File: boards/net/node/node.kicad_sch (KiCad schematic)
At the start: 60 parts, among them J1 N, J2 E, J3 S, J4 W, J5 SENSOR, J6 PROG, SW1 SW-18010P, U1 RP2040, U2 W25Q16JVSSIQ, U3 VL53L0CXV0DH/1, U4 ME6211C33M5G, Y1 12MHz

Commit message: net/node: link connectors centred and aligned for tiling; U1 caps to 0402
J1..J4 now sit with pin 2 exactly on each edge's centre line (24.0 on
the 48 x 48 board), so a node's W/S connectors line up with its
neighbours' E/N connectors when the net is tiled by translation.
pcb.py derives the rows from the board centre and refuses to generate
a board whose facing rows are misaligned or off-centre.

To free the west edge for J4, the U1 decoupling caps C10/C15 (100 nF,
C307331) and C11/C13 (1 uF, C52923) are now 0402, packed beside pins
43-45: pin-to-cap tracks went from 2.6-8.0 mm to 1.4-2.9 mm. C9 moved
0.5 mm and DM/DP re-routed; R15/R16, the crystal, pogo pads and M2
holes are unchanged. J5 moved 0.07 mm east to clear J3's courtyard,
leaving two silk_edge_clearance warnings (documented).

README: tiling rule and half-twist cable note, 0402 decision, variant
BOM command groups like the jobset so 0402/0603 parts stay separate.

Co-Authored-By: Claude Opus 5.5 <noreply@anthropic.com>
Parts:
- C10, C15: footprint Capacitor_SMD:C_0603_1608Metric -> Capacitor_SMD:C_0402_1005Metric; LCSC C14663 -> C307331; MPN CC0603KRX7R9BB104 -> CL05B104KB54PNC; Manufacturer Yageo -> Samsung
- C11, C13: footprint Capacitor_SMD:C_0603_1608Metric -> Capacitor_SMD:C_0402_1005Metric; LCSC C15849 -> C52923; MPN CL10A105KB8NNNC -> CL05A105KA5NQNC
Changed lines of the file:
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@@
 			)
 		)
-		(property "Footprint" "Capacitor_SMD:C_0603_1608Metric"
+		(property "Footprint" "Capacitor_SMD:C_0402_1005Metric"
 			(at 99.06 205.74 0)
 			(effects
@@
 			)
 		)
-		(property "Description" "100 nF X7R 50 V"
+		(property "Description" "100 nF X7R 50 V 0402"
 			(at 99.06 205.74 0)
 			(effects
@@
 			)
 		)
-		(property "MPN" "CC0603KRX7R9BB104"
+		(property "MPN" "CL05B104KB54PNC"
 			(at 99.06 205.74 0)
 			(effects
@@
 			)
 		)
-		(property "Manufacturer" "Yageo"
+		(property "Manufacturer" "Samsung"
 			(at 99.06 205.74 0)
 			(effects
@@
 			)
 		)
-		(property "LCSC" "C14663"
+		(property "LCSC" "C307331"
 			(at 99.06 205.74 0)
 			(effects
@@
 			)
 		)
-		(property "Footprint" "Capacitor_SMD:C_0603_1608Metric"
+		(property "Footprint" "Capacitor_SMD:C_0402_1005Metric"
 			(at 106.68 205.74 0)
 			(effects
@@
 			)
 		)
-		(property "Description" "1 uF X5R 50 V"
+		(property "Description" "1 uF X5R 25 V 0402"
 			(at 106.68 205.74 0)
 			(effects
@@
 			)
 		)
-		(property "MPN" "CL10A105KB8NNNC"
+		(property "MPN" "CL05A105KA5NQNC"
 			(at 106.68 205.74 0)
 			(effects
@@
 			)
 		)
-		(property "LCSC" "C15849"
+		(property "LCSC" "C52923"
 			(at 106.68 205.74 0)
 			(effects
@@
 			)
 		)
-		(property "Footprint" "Capacitor_SMD:C_0603_1608Metric"
+		(property "Footprint" "Capacitor_SMD:C_0402_1005Metric"
 			(at 127 205.74 0)
 			(effects
@@
 			)
 		)
-		(property "Description" "1 uF X5R 50 V"
+		(property "Description" "1 uF X5R 25 V 0402"
 			(at 127 205.74 0)
 			(effects
@@
 			)
 		)
-		(property "MPN" "CL10A105KB8NNNC"
+		(property "MPN" "CL05A105KA5NQNC"
 			(at 127 205.74 0)
 			(effects
@@
 			)
 		)
-		(property "LCSC" "C15849"
+		(property "LCSC" "C52923"
 			(at 127 205.74 0)
 			(effects
@@
 			)
 		)
-		(property "Footprint" "Capacitor_SMD:C_0603_1608Metric"
+		(property "Footprint" "Capacitor_SMD:C_0402_1005Metric"
 			(at 142.24 205.74 0)
 			(effects
@@
 			)
 		)
-		(property "Description" "100 nF X7R 50 V"
+		(property "Description" "100 nF X7R 50 V 0402"
 			(at 142.24 205.74 0)
 			(effects
@@
 			)
 		)
-		(property "MPN" "CC0603KRX7R9BB104"
+		(property "MPN" "CL05B104KB54PNC"
 			(at 142.24 205.74 0)
 			(effects
@@
 			)
 		)
-		(property "Manufacturer" "Yageo"
+		(property "Manufacturer" "Samsung"
 			(at 142.24 205.74 0)
 			(effects
@@
 			)
 		)
-		(property "LCSC" "C14663"
+		(property "LCSC" "C307331"
 			(at 142.24 205.74 0)
 			(effects

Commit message: net/node: re-floorplan (MCU centre, peripherals in corners); J5 removed
U1 (rotated 180) and its support (decoupling, crystal, flash, LDO,
USB series R) now fill the centre between the four edge-centred link
connectors; peripherals take the corners: BZ1 NE, VL53L0X SE, pogo
pads J6 SW, SW1 NW. LED D2 sits just NE of U1. The 5 V ring is closed.

J5 (1x7 sensor header) is removed: its courtyard fits no corner and it
carried the longest run (SENS_AIN). GPIO26 is a no-connect; the bare
variant is now a sensorless relay node.

Mounting holes: no pad, via or footprint within 3.7 mm of a hole
centre (C2 had been 3.08 mm from H1; an M2 washer is 5 mm OD),
enforced by annulus keepouts (pcbgen.keepout r_in/pads/footprints/
tracks) and a pcb.py assertion. Crystal copper 23.3 -> 16.2 mm, USB
pair ~26 -> ~23 mm; make check: 0 violations, 0 warnings.

Co-Authored-By: Claude Opus 5.5 <noreply@anthropic.com>
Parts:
- removed J5: SENSOR, Connector_PinHeader_2.54mm:PinHeader_1x07_P2.54mm_Vertical, symbol Connector_Generic:Conn_01x07
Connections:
- net SENS_AIN: no longer names the net of U1.38 (GPIO26/ADC0)
- no-connect marks 21 -> 22
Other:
- note added: "Sensor. U3 = default variant, SW1 = "vib" variant, "bare" = no sensor (relay-only node)."
- note removed: "Sensor port. J5 takes off-board modules (LD2410, AM312 PIR, I2C breakouts). U3 = default variant, SW1 = "vib" variant, "bare" = header only."
- title: Net node: RP2040, 4 neighbour links, RGB LED, piezo, sensor port -> Net node: RP2040, 4 neighbour links, RGB LED, piezo, sensor

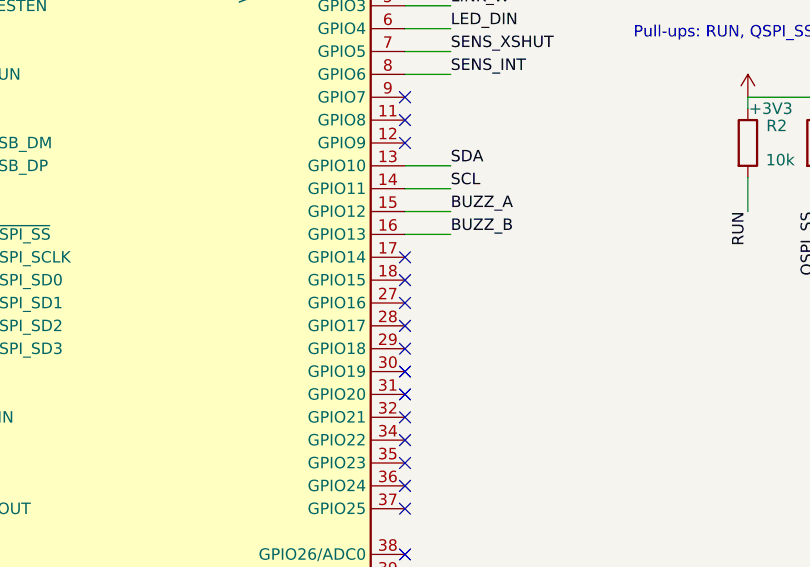
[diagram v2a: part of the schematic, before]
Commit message: net/node: isolate the crystal (buzzer to GPIO18/19, guard pour, 1 mm rule); J6 centred
The piezo drive moved from GPIO12/13 (pins 15/16, four pins from
XIN/XOUT) to GPIO18/19 (PWM slice 1 A/B, pins 29/30), routed on B.Cu
under U1 to BZ1; BUZZ_B went from 0.55 to 2.0 mm from crystal copper.

Every other non-GND net now keeps >= 1.0 mm (same layer, edge to edge)
from the crystal nets and the LED nets and all D4 pads >= 2.0 mm,
checked by generate/xtal_check.py (tracks, arcs with sagitta margin,
vias, pads, zones; rejects unmodelled copper) and asserted from
pcb.py. Known exemption: the IOVDD/DVDD escapes inside U1's pin field.
A notched F.Cu GND guard pour surrounds Y1/C1/C2/R1, stitched to In1
by 19 vias, asserted free of foreign copper. C19 now sits at D2's VDD
pin (LED loop 15.5 -> 8.7 mm).

J6 pogo pads centred in the SW corner (margins to J3/J4/H3 ring
0.57/0.58/0.60 mm); USB pair 22.0/19.8 mm; README jig coordinates
updated. make check: 0 violations, 0 warnings.

Co-Authored-By: Claude Opus 5.5 <noreply@anthropic.com>
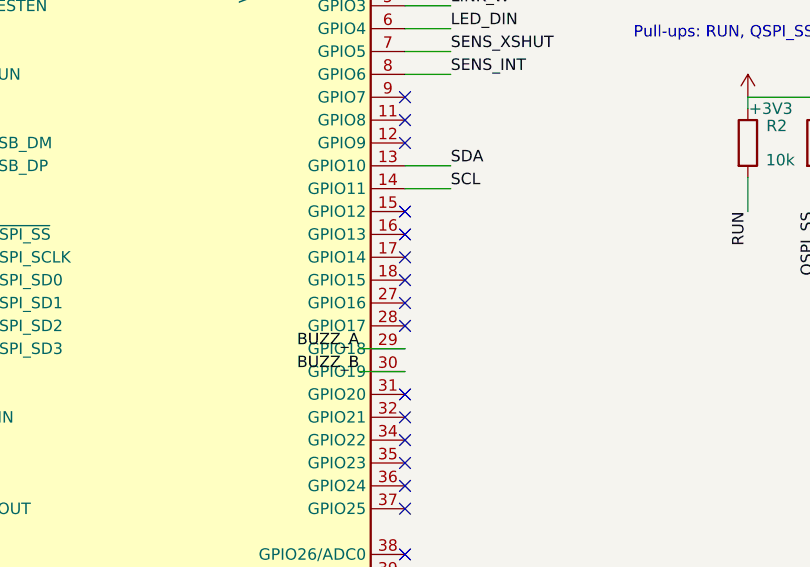
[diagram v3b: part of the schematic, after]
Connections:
- net BUZZ_A: now also U1.29 (GPIO18); no longer U1.15 (GPIO12)
- net BUZZ_B: now also U1.30 (GPIO19); no longer U1.16 (GPIO13)
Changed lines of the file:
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@@
 	(wire
 		(pts
-			(xy 139.7 119.38)
-			(xy 144.78 119.38)
+			(xy 139.7 134.62)
+			(xy 134.62 134.62)
 		)
 		(stroke
@@
 	)
 	(label "BUZZ_A"
-		(at 144.78 119.38 0)
-		(effects
-			(font
-				(size 1.27 1.27)
-			)
-			(justify left bottom)
-		)
-	)
-	(wire
-		(pts
-			(xy 139.7 121.92)
-			(xy 144.78 121.92)
+		(at 134.62 134.62 180)
+		(effects
+			(font
+				(size 1.27 1.27)
+			)
+			(justify right bottom)
+		)
+	)
+	(wire
+		(pts
+			(xy 139.7 137.16)
+			(xy 134.62 137.16)
 		)
 		(stroke
@@
 	)
 	(label "BUZZ_B"
-		(at 144.78 121.92 0)
-		(effects
-			(font
-				(size 1.27 1.27)
-			)
-			(justify left bottom)
+		(at 134.62 137.16 180)
+		(effects
+			(font
+				(size 1.27 1.27)
+			)
+			(justify right bottom)
 		)
 	)
@@
 	)
 	(no_connect
+		(at 139.7 119.38)
+	)
+	(no_connect
+		(at 139.7 121.92)
+	)
+	(no_connect
 		(at 139.7 124.46)
 	)
@@
 	)
 	(no_connect
-		(at 139.7 134.62)
-	)
-	(no_connect
-		(at 139.7 137.16)
-	)
-	(no_connect

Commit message: net/node: four corner LEDs; pre-order panel fixes (BOOT 1k, TVS, USB Schottky)
Four WS2812B-2020-V6 (D1..D4, C52917434), one per corner, 4.0 mm in
from an edge and 8.8 mm from the corner, chained NE->NW->SW->SE on
GPIO4, so a node shows the direction a pattern moves (2x2 sub-pixels).
Each has its own 100 nF 0402. The LEDs run from +5V through
U5 SN74AHCT1G125 (C7484) as level shifter; the 1N4148W drop diode is
gone (at LED idle current it no longer guaranteed VIH). Board stays
48 x 48; budget ~215 mA/node full white.

Fixes from the cross-model pre-order review:
- R19 1 k between QSPI_SS and the BOOT pogo pad, at the flash (RP2040
  hardware design guide p.9); J6.8 no longer shorts QSPI_SS.
- D5 SMF5.0A TVS on +5V at the LDO input (energy sink; limits
  documented, measure the plug transient on first boards).
- D6 B5819W from the jig's USB 5 V to +5V, so a powered net cannot
  backfeed the host.
- J1-J4 and SW1 out of the position files (hand-soldered);
  pcbgen carries base exclusions into variants (+ test).
- J6 vias moved out of the pogo pads; piezo drive modes without DC.

make check: 0 violations, 0 warnings; make parts --boards 30 clean.

Co-Authored-By: Claude Opus 5.5 <noreply@anthropic.com>
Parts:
- removed D1: 1N4148W, Diode_SMD:D_SOD-123, symbol Device:D
- added C23, C24, C25, C26: 100n, Capacitor_SMD:C_0402_1005Metric, symbol Device:C
- added D1, D3: WS2812B-2020-V6, LED_SMD:LED_WS2812B-2020_PLCC4_2.0x2.0mm, symbol LED:WS2812B-2020
- added D5: SMF5.0A, Diode_SMD:D_SOD-123F, symbol Device:D_Zener
- added D6: B5819W, Diode_SMD:D_SOD-123, symbol Device:D_Schottky
- added R19: 1k, Resistor_SMD:R_0603_1608Metric, symbol Device:R
- added U5: 74AHCT1G125, Package_TO_SOT_SMD:SOT-23-5, symbol 74xGxx:74AHCT1G125
- C19: footprint Capacitor_SMD:C_0603_1608Metric -> Capacitor_SMD:C_0402_1005Metric; LCSC C14663 -> C307331; MPN CC0603KRX7R9BB104 -> CL05B104KB54PNC; Manufacturer Yageo -> Samsung
- D4: now fitted
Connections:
- net LED_VDD is gone; now on net +5V: C19.1, D2.4 (VDD), D4.4 (VDD)
- net +5V: now also C23.1, C24.1, C25.1, C26.1, D1.4 (VDD), D3.4 (VDD), D5.1 (K), D6.1 (K), U5.5 (VCC); no longer J6.7 (Pin_7)
- net GND: now also C23.2, C24.2, C25.2, C26.2, D1.2 (VSS), D3.2 (VSS), D5.2 (A), U5.1, U5.3 (GND)
- net LED_DIN: now also D1.3 (DIN), U5.4; no longer D2.3 (DIN), U1.6 (GPIO4)
- net QSPI_SS: now also R19.1; no longer J6.8 (Pin_8)
- net LED_CH2: now reaches D2.1 (DOUT)
- net LED_CH2: now also D3.3 (DIN); no longer D4.3 (DIN)
- new net: D6.2 (A), J6.7 (Pin_7)
- new net BOOT: J6.8 (Pin_8), R19.2
- new net LED_CH1: D1.1 (DOUT), D2.3 (DIN)
- new net LED_CH3: D3.1 (DOUT), D4.3 (DIN)
- new net LED_DATA: U1.6 (GPIO4), U5.2
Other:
- note added: "Corner LEDs, chain D1 NE -> D2 NW -> D3 SW -> D4 SE (pixel 0..3), all on +5V. U5 (AHCT, VIH 2.0 V) shifts the 3.3 V data to 5 V: WS2812B-2020-V6 VIH = 0.55 VDD."
- note removed: "D1 drops the LED supply to ~4.3 V: WS2812B-2020-V6 VIH is 0.55 VDD (2.4 V), so 3.3 V logic has margin. D4 is DNP: fit it for a brighter node."
- title: Net node: RP2040, 4 neighbour links, RGB LED, piezo, sensor -> Net node: RP2040, 4 neighbour links, 4 corner RGB LEDs, piezo, sensor

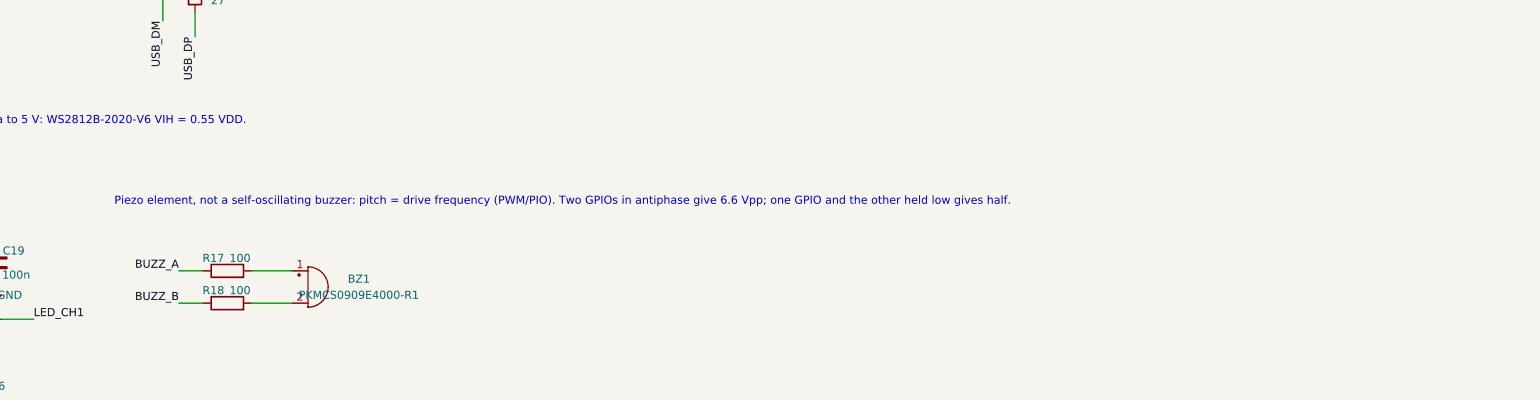
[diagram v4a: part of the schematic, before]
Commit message: docs: resume context for net/node ordering and this session's tooling lessons
net/node README: status now "reviewed, ready to order pending the
owner's GUI check and quote", with the pre-order panel outcome; the
Resume path has the order checklist (upload paths, hand-soldered
J1..J4 unselected, first-batch recommendation, loose parts, cable
direction and continuity test, supply sizing and hot-plug caution)
and how to render / get 3D models. Power paragraph updated to the
four-LED budget; the schematic's piezo note no longer suggests a DC
drive mode.

CLAUDE.md: worktree-per-change workflow with concurrent sessions,
Codex resume by session id, the pre-order panel (Gemini weighted 1/4),
the CI $HOME/.cache fix, KiCad 10 variant pos-file quirk, hole-clearance
annulus keepouts, crystal isolation checker, RP2040/WS2812B-V6 facts,
keep vias out of pogo pads, correct output paths, review history and
ideas-list updates. Root README board table and .gitignore (.history/).

Co-Authored-By: Claude Opus 5.5 <noreply@anthropic.com>
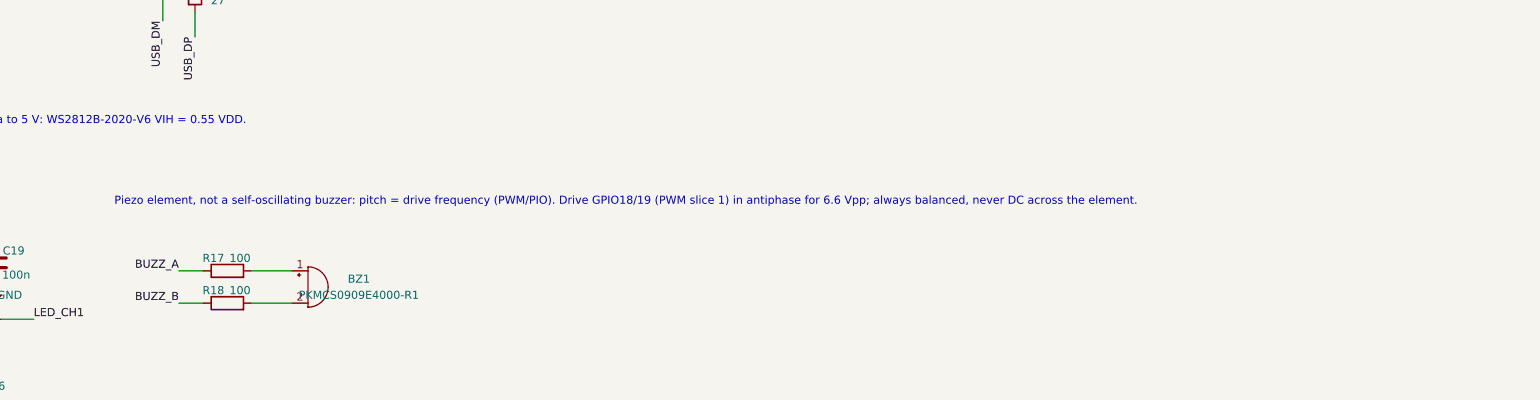
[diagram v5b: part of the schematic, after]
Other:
- note added: "Piezo element, not a self-oscillating buzzer: pitch = drive frequency (PWM/PIO). Drive GPIO18/19 (PWM slice 1) in antiphase for 6.6 Vpp; always balanced, never DC across the element."
- note removed: "Piezo element, not a self-oscillating buzzer: pitch = drive frequency (PWM/PIO). Two GPIOs in antiphase give 6.6 Vpp; one GPIO and the other held low gives half."
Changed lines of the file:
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@@
 		)
 	)
-	(text "Piezo element, not a self-oscillating buzzer: pitch = drive frequency (PWM/PIO). Two GPIOs in antiphase give 6.6 Vpp; one GPIO and the other held low gives half."
+	(text "Piezo element, not a self-oscillating buzzer: pitch = drive frequency (PWM/PIO). Drive GPIO18/19 (PWM slice 1) in antiphase for 6.6 Vpp; always balanced, never DC across the element."
 		(exclude_from_sim no)
 		(at 350.52 104.14 0)
